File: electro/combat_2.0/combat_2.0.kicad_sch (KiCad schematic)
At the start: 11 parts, among them J1 Screw_Terminal_01x02, J5 Conn_01x03_Pin, U1 NodeMCU1.0(ESP-12E), U2 AZ1117CH-5.0TRG1

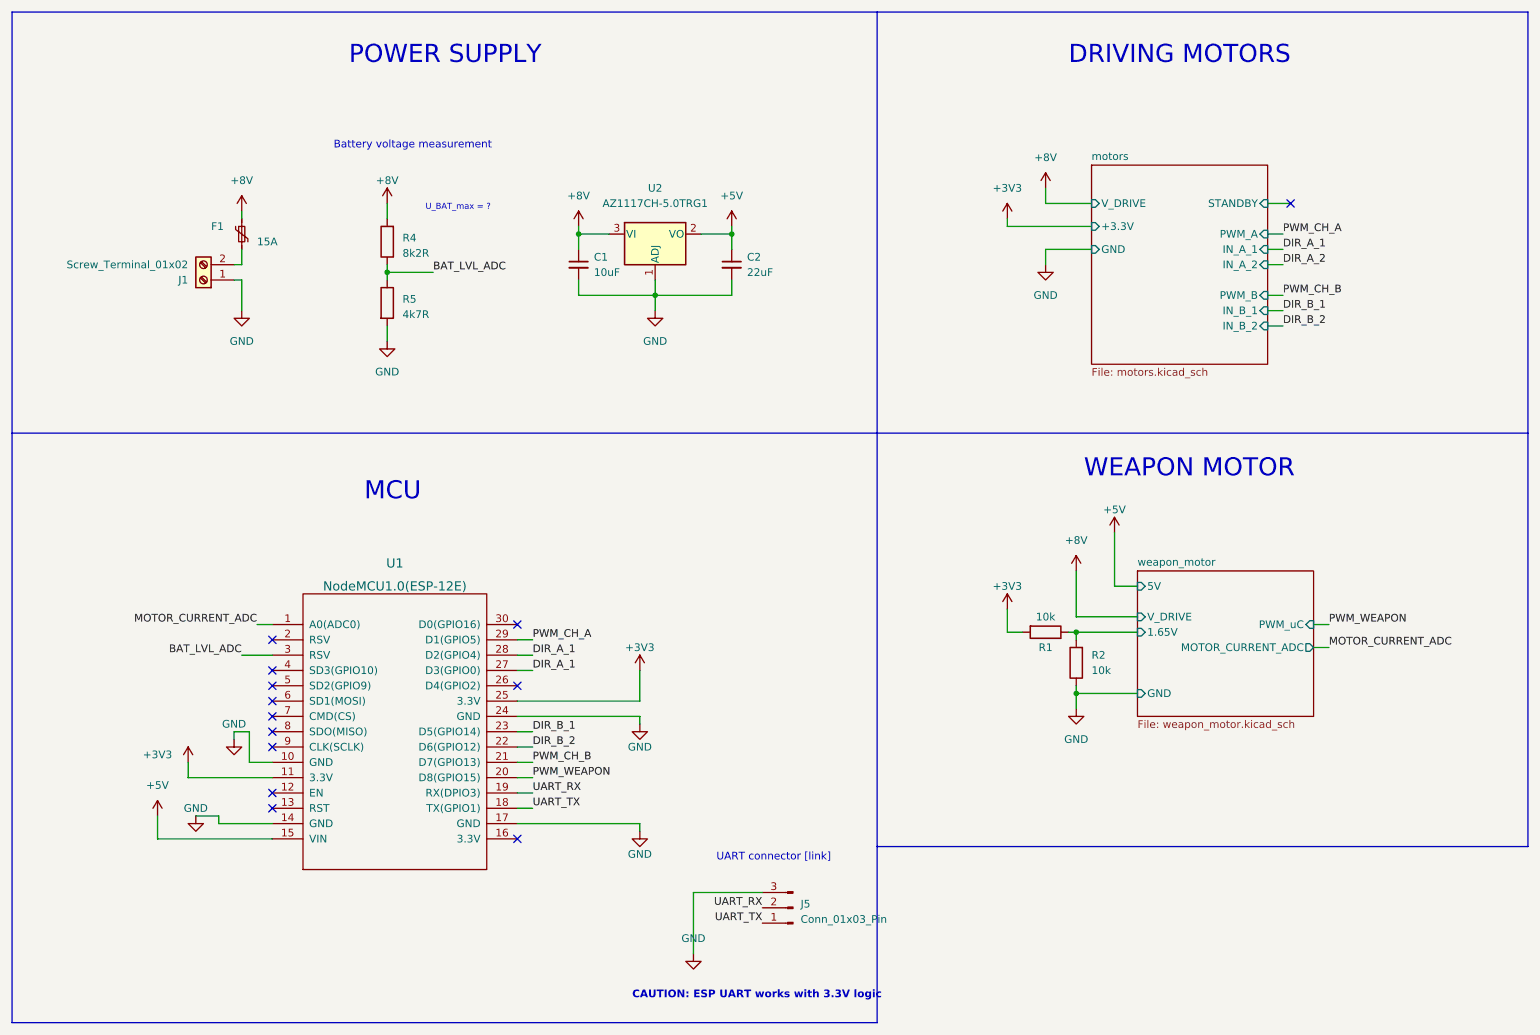
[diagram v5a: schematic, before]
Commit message: Changed MCU to ESP32-DEVKITC, cleared some ERC errors
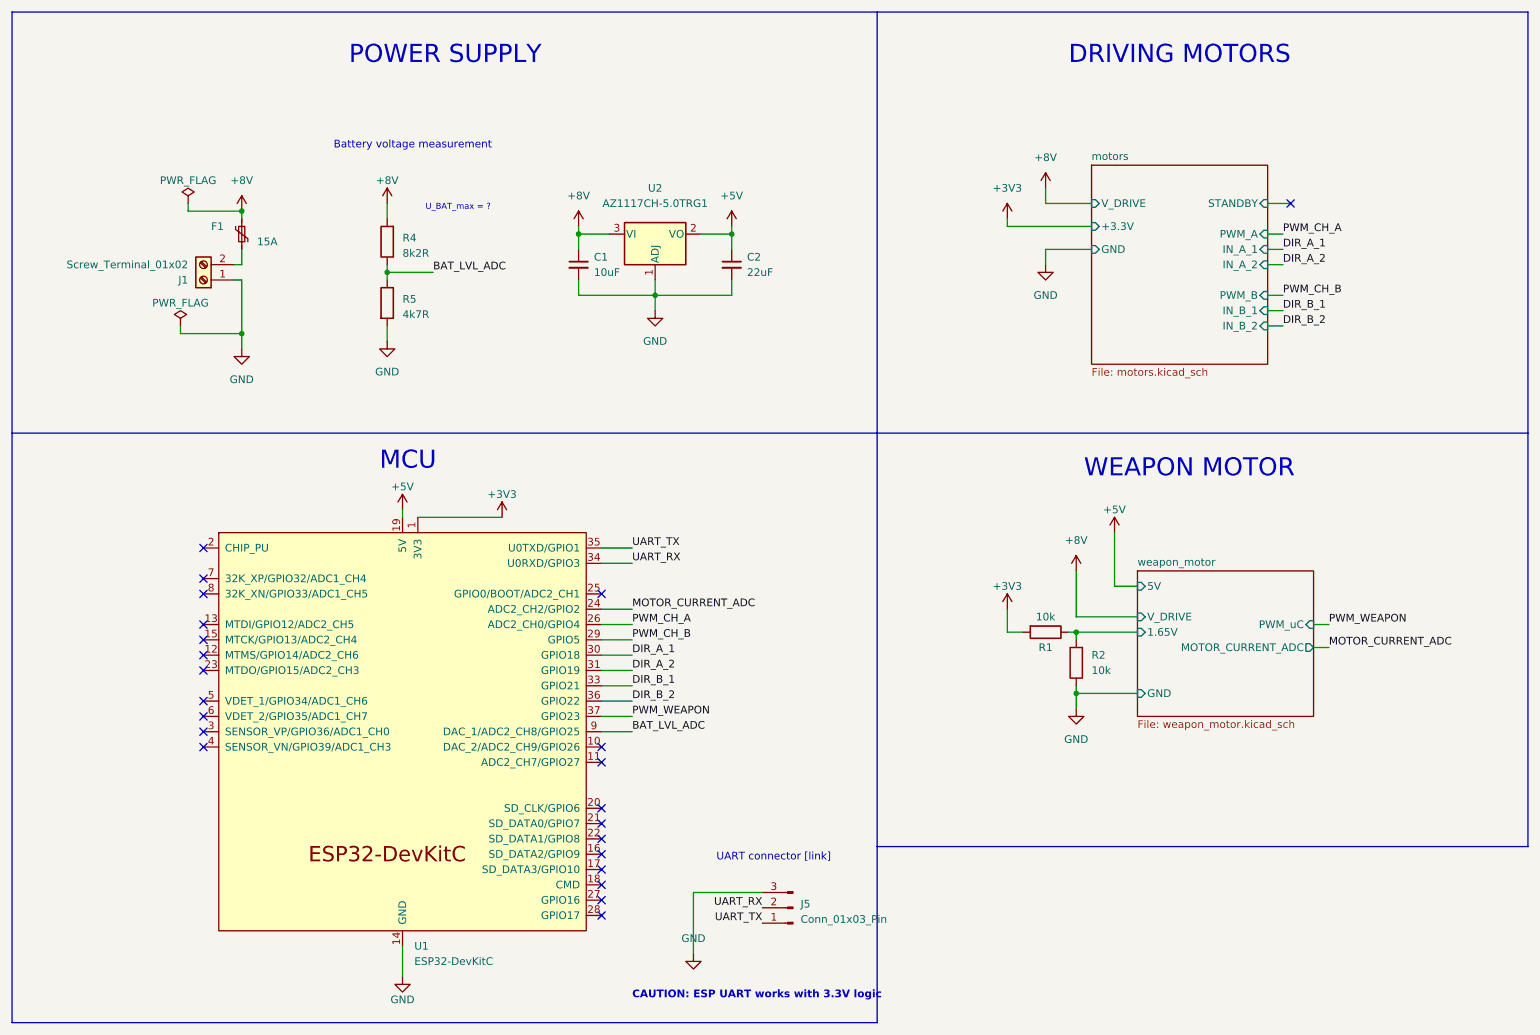
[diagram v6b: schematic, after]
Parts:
- removed U1: NodeMCU1.0(ESP-12E), ESP8266:ESP12F-Devkit-V3, symbol ESP8266:NodeMCU1.0(ESP-12E)
- added U1: ESP32-DevKitC, Espressif:ESP32-DevKitC, symbol Espressif:ESP32-DevKitC
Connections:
- net +3V3: now also U1.1 (3V3)
- net +5V: now also U1.19 (5V)
- net BAT_LVL_ADC: now also U1.9 (DAC_1/ADC2_CH8/GPIO25)
- net DIR_A_1: now also U1.30 (GPIO18)
- net DIR_A_2: now also U1.31 (GPIO19)
- net DIR_B_1: now also U1.33 (GPIO21)
- net DIR_B_2: now also U1.36 (GPIO22)
- net GND: now also U1.14 (GND), U1.32 (GND), U1.38 (GND)
- net MOTOR_CURRENT_ADC: now also U1.24 (ADC2_CH2/GPIO2)
- net PWM_CH_A: now also U1.26 (ADC2_CH0/GPIO4)
- net PWM_CH_B: now also U1.29 (GPIO5)
- net PWM_WEAPON: now also U1.37 (GPIO23)
- net UART_RX: now also U1.34 (U0RXD/GPIO3)
- net UART_TX: now also U1.35 (U0TXD/GPIO1)
- no-connect marks 13 -> 23

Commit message: Updated some footprints
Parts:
- C1, C2: footprint Capacitor_SMD:C_0805_2012Metric -> Capacitor_SMD:C_1206_3216Metric_Pad1.33x1.80mm_HandSolder
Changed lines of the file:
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@@
       (effects (font (size 1.27 1.27)) (justify left))
     )
-    (property "Footprint" "Capacitor_SMD:C_0805_2012Metric" (at 142.24 60.96 0)
+    (property "Footprint" "Capacitor_SMD:C_1206_3216Metric_Pad1.33x1.80mm_HandSolder" (at 142.24 60.96 0)
       (effects (font (size 1.27 1.27)) hide)
     )
@@
       (effects (font (size 1.27 1.27)) (justify left))
     )
-    (property "Footprint" "Capacitor_SMD:C_0805_2012Metric" (at 116.84 60.96 0)
-      (effects (font (size 1.27 1.27)) hide)
-    )
+    (property "Footprint" "Capacitor_SMD:C_1206_3216Metric_Pad1.33x1.80mm_HandSolder" (at 116.84 60.96 0)
+      (effects (font (size 1.27 1.27)) hide)
+    )

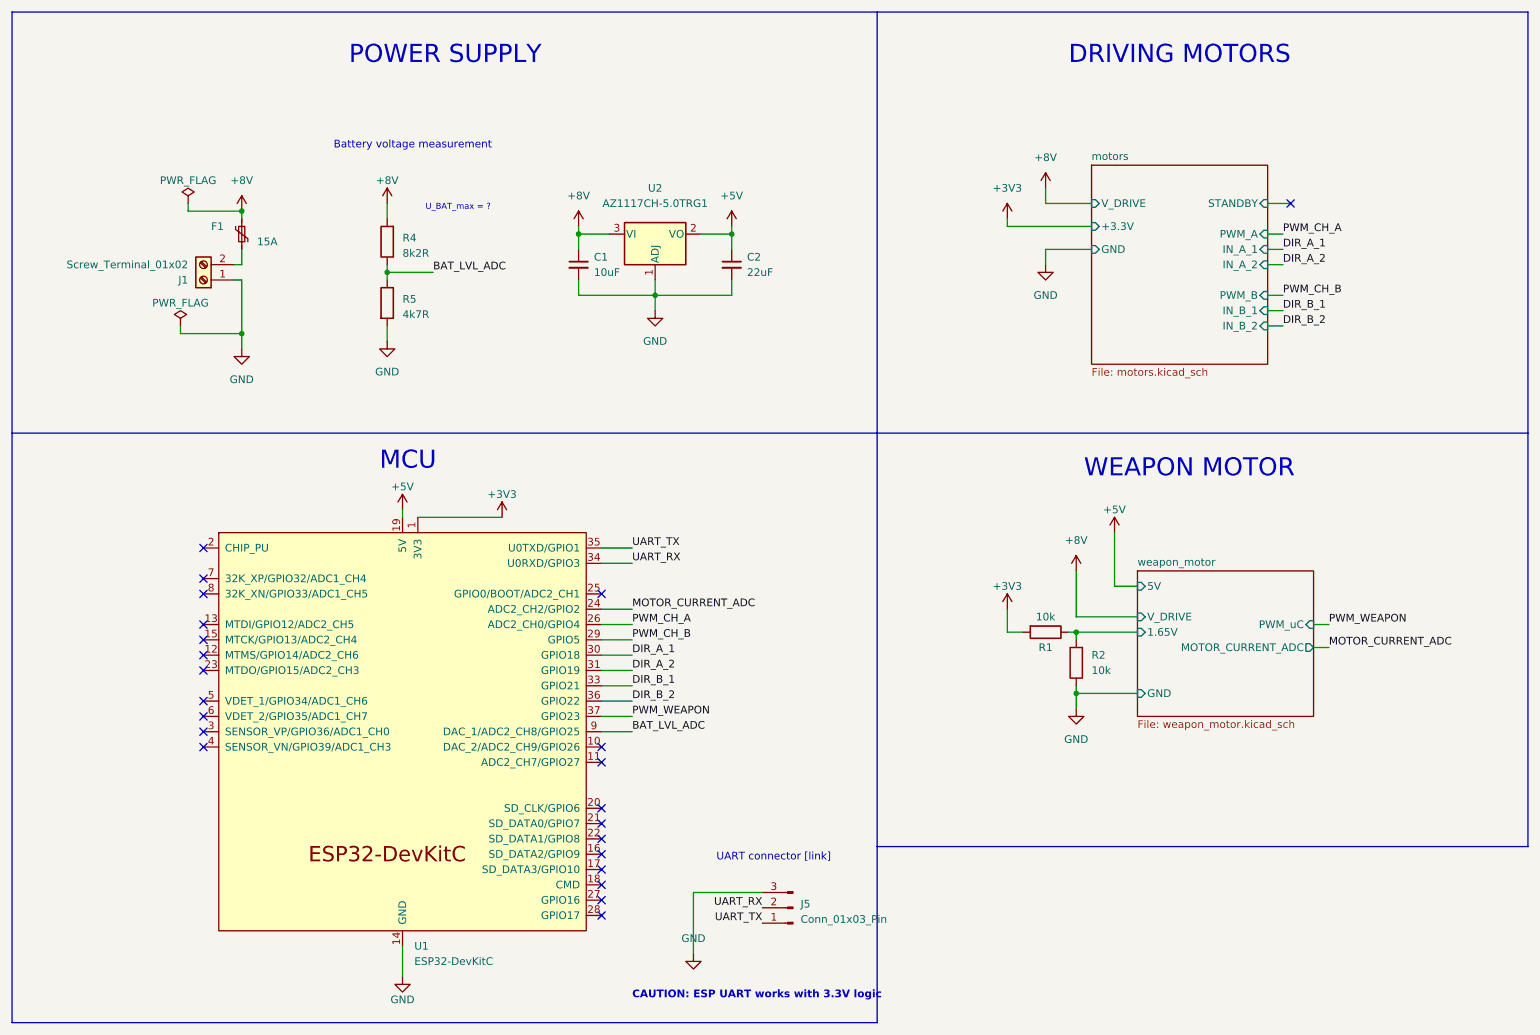
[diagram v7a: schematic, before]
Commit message: Changed Devkit for ESP32-WROOM device. Added LDO, some other peripherals
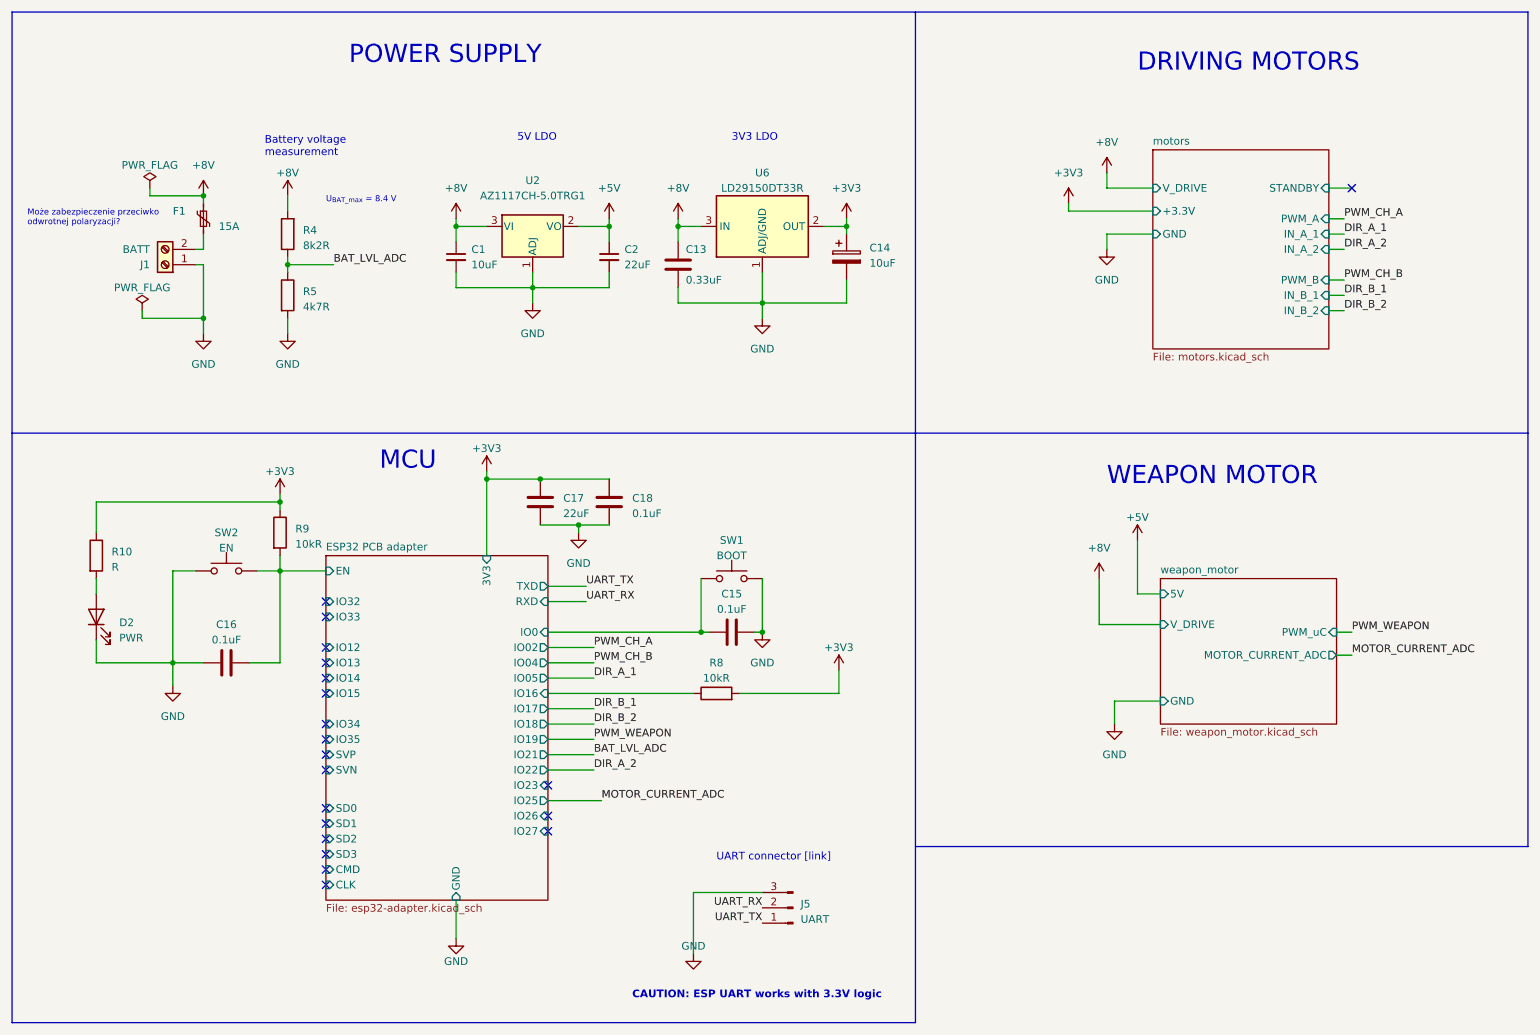
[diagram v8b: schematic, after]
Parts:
- removed R1, R2: 10k, Resistor_SMD:R_1206_3216Metric_Pad1.30x1.75mm_HandSolder, symbol Device:R
- removed U1: ESP32-DevKitC, Espressif:ESP32-DevKitC, symbol Espressif:ESP32-DevKitC
- added C13: 0.33uF, Capacitor_SMD:C_1206_3216Metric_Pad1.33x1.80mm_HandSolder, symbol Device:C
- added C14: 10uF, Capacitor_SMD:CP_Elec_4x5.4, symbol Device:C_Polarized
- added C15, C16, C18: 0.1uF, Capacitor_SMD:C_1206_3216Metric_Pad1.33x1.80mm_HandSolder, symbol Device:C
- added C17: 22uF, Capacitor_SMD:C_1206_3216Metric_Pad1.33x1.80mm_HandSolder, symbol Device:C
- added D2: PWR, LED_SMD:LED_1206_3216Metric_Pad1.42x1.75mm_HandSolder, symbol Device:LED
- added R10: R, Resistor_SMD:R_1206_3216Metric_Pad1.30x1.75mm_HandSolder, symbol Device:R
- added R8, R9: 10kR, Resistor_SMD:R_1206_3216Metric_Pad1.30x1.75mm_HandSolder, symbol Device:R
- added SW1: BOOT, Button_Switch_SMD:SW_Push_1P1T_NO_CK_KMR2, symbol Switch:SW_Push
- added SW2: EN, Button_Switch_SMD:SW_Push_1P1T_NO_CK_KMR2, symbol Switch:SW_Push
- added U6: LD29150DT33R, Package_TO_SOT_SMD:TO-252-2, symbol Regulator_Linear:LD1086DT33TR
- J1: value Screw_Terminal_01x02 -> BATT
- J5: value Conn_01x03_Pin -> UART
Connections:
- net +3V3: now also C14.1, C17.1, C18.1, R10.1, R8.2, R9.1, U6.2 (OUT)
- net +8V: now also C13.1, U6.3 (IN)
- net GND: now also C13.2, C14.2, C15.2, C16.1, C17.2, C18.2, D2.1 (K), SW1.2, SW2.1, U6.1 (ADJ/GND)
- new net: D2.2 (A), R10.2
- new net ESP32 PCB adapter/EN: C16.2, R9.2, SW2.2
- new net ESP32 PCB adapter/IO0: C15.1, SW1.1
- new net ESP32 PCB adapter/IO16: R8.1
- no-connect marks 23 -> 20
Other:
- added sheet ESP32 PCB adapter (esp32-adapter.kicad_sch)
- sheet weapon_motor ports: added none; removed 1.65V
- note added: "3V3 LDO"
- note added: "5V LDO"
- note added: "Może zabezpieczenie przeciwko odwrotnej polaryzacji?"
- note added: "U_{BAT_max} = 8.4 V"
- note removed: "U_BAT_max = ?"
- moved on the sheet: C1, C2, F1, J1, R4, R5, U2
